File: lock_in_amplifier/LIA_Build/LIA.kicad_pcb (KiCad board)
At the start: 2 copper layers, 140 parts, among them J1 vref-in, J10 A IN COAX, J11 B IN, J13 A IN, J14 I IN COAX, J15 I IN, J16 TEST SIGNAL OUT, J17 RF_Shield_One_Piece, J18 TEST HIGH SIDE VALUE, J19 +3V3 OUT, J2 vref, J20 AMP OUT, J21 AMP OUT COAX, J22 CLK IN, J23 CLK IN COAX, J26 CLK OUT, J27 CLK OUT COAX, J3 V-IN, J30 DEMOD OUT - I, J31 DEMOD OUT I COAX, J32 DEMOD OUT Q COAX, J33 DEMOD OUT - Q, J34 DEMOD PROG, J38 RF_Shield_One_Piece, J39 BOOT, J4 GND, J42 VOCM, J46 -5V OUT, J47 +5V OUT, J48 XOUT, J5 V+IN, J6 +5V, J7 +3V3, J8 -5V, J9 B IN COAX, Q1 DMN640L, Q2 DMN640L, U1 LM358, U11 ADA2200, U6 lmp7721, U7 OP1177, U8 AD8429, U9 OP1177

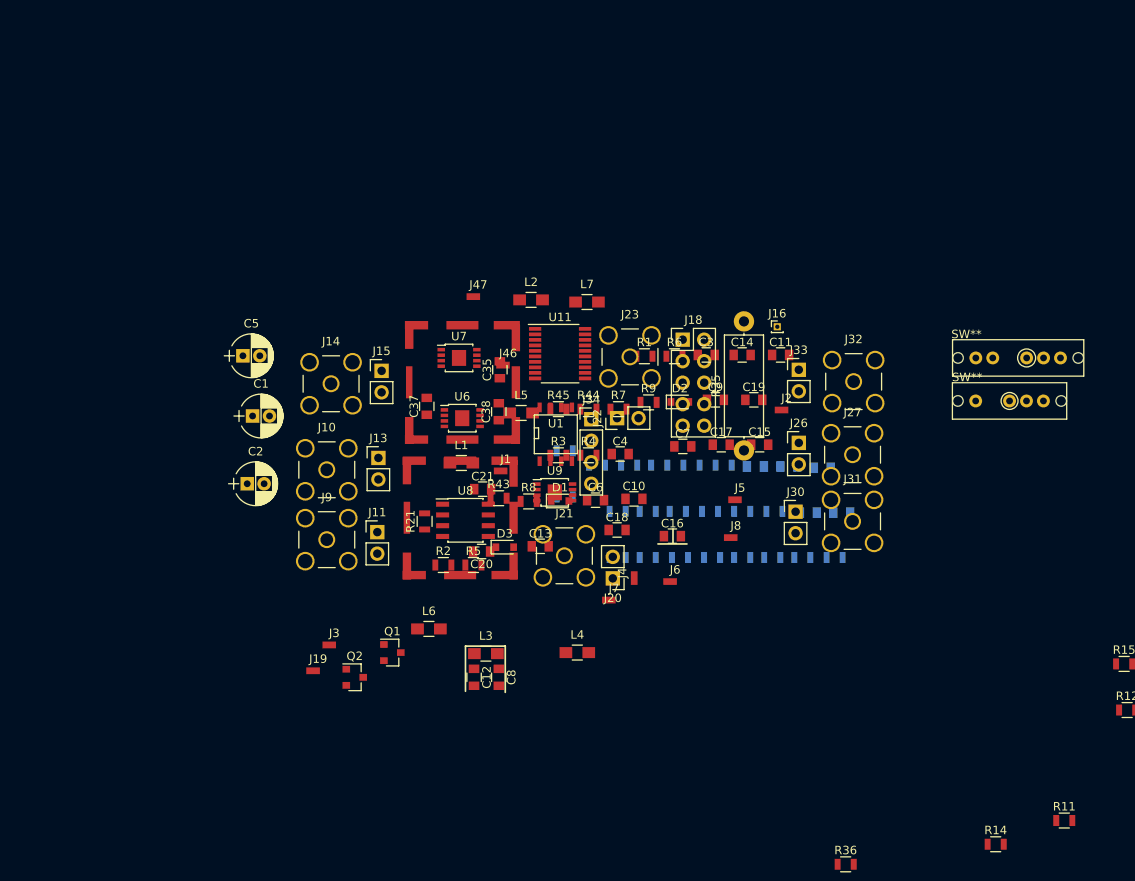
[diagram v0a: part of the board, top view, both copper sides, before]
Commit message: PLL initial implementation
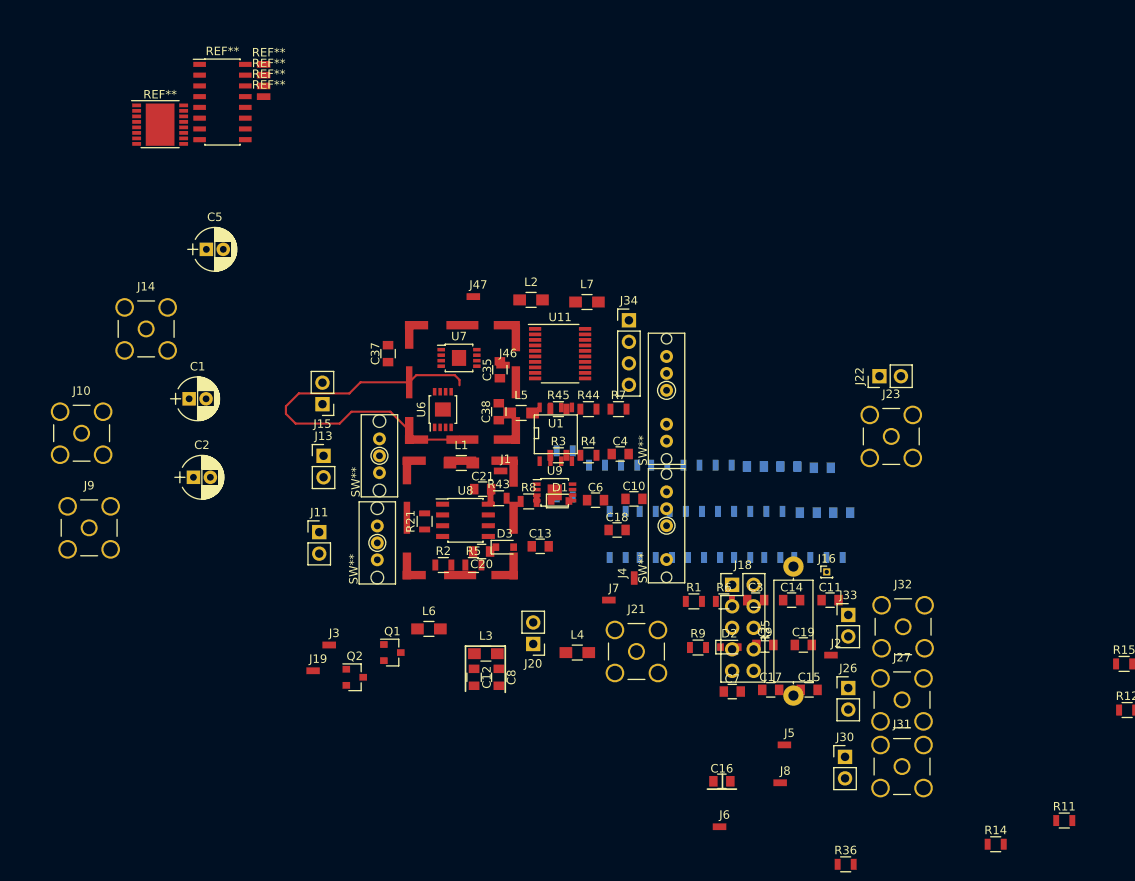
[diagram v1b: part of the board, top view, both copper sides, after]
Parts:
- added REF**: tyco_RC_0603_Probe_Pad, footprints:tyco_RCU_0603_Probe_Pad, F.Cu at (146.4, -4.06)
- added REF**: tyco_RC_0603_Probe_Pad, footprints:tyco_RCU_0603_Probe_Pad, F.Cu at (146.4, -2.79)
- added REF**: HTSSOP-16-1EP_4.4x5mm_Pitch0.65mm, Housings_SSOP:HTSSOP-16-1EP_4.4x5mm_Pitch0.65mm, F.Cu at (133.6, 2.41)
- added REF**: SOIC-16_3.9x9.9mm_Pitch1.27mm, Housings_SOIC:SOIC-16_3.9x9.9mm_Pitch1.27mm, F.Cu at (141.0, -0.25)
- added REF**: tyco_RC_0603_Probe_Pad, footprints:tyco_RCU_0603_Probe_Pad, F.Cu at (146.4, -6.60)
- added REF**: tyco_RC_0603_Probe_Pad, footprints:tyco_RCU_0603_Probe_Pad, F.Cu at (146.4, -5.33)
- added SW**: SPDT, footprints:SPDT_OS102011MS2QN1, F.Cu at (159.5, 41.5)
- added SW**: SPDT, footprints:SPDT_OS102011MS2QN1, F.Cu at (159.3, 51.8)
- moved SW** 43.1 mm to (193.4, 49.8), turned to 90 degrees
- moved SW** 41.8 mm to (193.4, 34.8), turned to 90 degrees
- moved J23 32.3 mm to (220.0, 39.2)
- moved J22 31.4 mm to (218.6, 32.1)
- moved C15 29.5 mm to (210.3, 69.2)
- moved J2 29.5 mm to (213.4, 63.2)
- moved J27 29.5 mm to (221.2, 70.4)
- moved R9 29.5 mm to (197.1, 64.2)
- moved C11 29.5 mm to (212.7, 58.6)
- moved C3 29.5 mm to (203.9, 58.6)
- moved J18 29.5 mm to (201.2, 56.8)
- moved R6 29.5 mm to (200.2, 58.7)
- moved C16 29.5 mm to (200.0, 80.0)
- moved C17 29.5 mm to (205.7, 69.2)
- moved C19 29.5 mm to (209.6, 63.9)
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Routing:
- net Net-(J17-Pad1): track 0.00 -> 46.2 mm

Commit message: started LNA test board.
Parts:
- removed REF** (x3): C_0603, Capacitors_SMD:C_0603
- removed REF** (x4): tyco_RC_0603_Probe_Pad, footprints:tyco_RCU_0603_Probe_Pad
- removed REF**: HTSSOP-16-1EP_4.4x5mm_Pitch0.65mm, Housings_SSOP:HTSSOP-16-1EP_4.4x5mm_Pitch0.65mm
- removed REF** (x2): C_0805, Capacitors_SMD:C_0805
- removed REF**: C_0402, Capacitors_SMD:C_0402
- removed REF**: SOIC-16_3.9x9.9mm_Pitch1.27mm, Housings_SOIC:SOIC-16_3.9x9.9mm_Pitch1.27mm
- removed SW** (x2): SPDT, footprints:SPDT_OS102011MS2QN1
- removed SW**: SP4T, footprints:SP4T_C&K_SS-14D0839-VG
- removed SW**: SP3T, footprints:SP3T_CK_SS-14D0839-VG
- added C25: 10pF, Capacitors_SMD:C_0805, F.Cu at (188.5, 69.4)
- added C27: 10pF, Capacitors_SMD:C_0805, F.Cu at (180.4, 74.9)
- added C31: 0.1uF, Capacitors_SMD:C_0805, F.Cu at (243.3, 87.8)
- added C32: 0.1uF, Capacitors_SMD:C_0805, F.Cu at (235.1, 98.1)
- added C33: 0.1uF, Capacitors_SMD:C_0805, F.Cu at (225.0, 108.9)
- added C34: 200pF, Capacitors_SMD:C_0805, F.Cu at (175.9, 76.6)
- added C36: 10pF, Capacitors_SMD:C_0805, F.Cu at (184.4, 69.6)
- added C39: C, Capacitors_SMD:C_0805, F.Cu at (185.6, 64.1)
- added C40: 10pF, Capacitors_SMD:C_0805, F.Cu at (176.4, 71.3)
- added C41: 270P, Capacitors_SMD:C_0805, F.Cu at (158.6, 124.8)
- added C42: 270P, Capacitors_SMD:C_0805, F.Cu at (174.4, 108.2)
- added C43: 270P, Capacitors_SMD:C_0805, F.Cu at (162.7, 119.4)
- added C44: 270P, Capacitors_SMD:C_0805, F.Cu at (182.6, 102.6)
- added C45: C, Capacitors_SMD:C_0805, F.Cu at (116.5, 49.0)
- added C46: C, Capacitors_SMD:C_0805, F.Cu at (105.5, 59.9)
- added C47: 100PF, Capacitors_SMD:C_0805, F.Cu at (101.8, 65.3)
- added C48: 0.1uF, Capacitors_SMD:C_0805, F.Cu at (98.0, 70.8)
- added C49: 0.1u, Capacitors_SMD:C_0805, F.Cu at (91.0, 76.2)
- added C50: 0.1u, Capacitors_SMD:C_0805, F.Cu at (109.4, 59.7)
- added C51: 0.1U, Capacitors_SMD:C_0805, F.Cu at (87.0, 74.5)
- added C52: 0.1U, Capacitors_SMD:C_0805, F.Cu at (112.5, 49.0)
- added C53: 0.1u, Capacitors_SMD:C_0805, F.Cu at (81.0, 87.3)
- added C54: 0.1u, Capacitors_SMD:C_0805, F.Cu at (239.5, 93.3)
- added C55: 0.1u, Capacitors_SMD:C_0805, F.Cu at (230.8, 98.1)
- added C56: 0.1u, Capacitors_SMD:C_0805, F.Cu at (120.4, 49.0)
- added C57: 0.1u, Capacitors_SMD:C_0805, F.Cu at (112.9, 54.3)
- added C58: 0.1u, Capacitors_SMD:C_0805, F.Cu at (86.0, 82.0)
- added C59: 0.1u, Capacitors_SMD:C_0805, F.Cu at (82.0, 82.0)
- added C60: C, Capacitors_SMD:C_0805, F.Cu at (109.0, 54.4)
- added D10: BAT54S, TO_SOT_Packages_SMD:SOT-23, F.Cu at (103.2, 129.5)
- added D11: BAT54S, TO_SOT_Packages_SMD:SOT-23, F.Cu at (109.1, 122.4)
- added D12: BAT54S, TO_SOT_Packages_SMD:SOT-23, F.Cu at (115.8, 110.1)
- added D13: BAT54S, TO_SOT_Packages_SMD:SOT-23, F.Cu at (103.2, 122.4)
- added D5: D, Diodes_SMD:D_0805, F.Cu at (226.7, 103.7)
- added D6: D, Diodes_SMD:D_0805, F.Cu at (207.7, 114.2)
- added D7: LED, LEDs:LED_0805, F.Cu at (231.0, 103.4)
- added D8: LED, LEDs:LED_0805, F.Cu at (85.2, 87.2)
- added D9: BAT54S, TO_SOT_Packages_SMD:SOT-23, F.Cu at (96.8, 131.7)
- added J12: POWER_IN, Pin_Headers:Pin_Header_Straight_1x03_Pitch2.54mm, F.Cu at (116.7, 98.1)
- added J24: BOOT, footprints:tyco_RCU_0603_Probe_Pad, F.Cu at (229.1, 108.2)
- added J25: VOCM, footprints:tyco_RCU_0603_Probe_Pad, F.Cu at (243.4, 92.4)
- added J28: DEMOD PROG, Pin_Headers:Pin_Header_Straight_1x04_Pitch2.54mm, F.Cu at (196.6, 103.0)
- added J29: XOUT, footprints:tyco_RCU_0603_Probe_Pad, F.Cu at (225.1, 113.5)
- added J35: rst, Pin_Headers:Pin_Header_Straight_1x02_Pitch2.54mm, F.Cu at (203.7, 107.8)
- added J36: DELAY SEL FINE, Pin_Headers:Pin_Header_Straight_1x10_Pitch2.54mm, F.Cu at (50.9, 49.8)
- added J37: DELAY SEL COARSE, Pin_Headers:Pin_Header_Straight_1x05_Pitch2.54mm, F.Cu at (64.4, 49.8)
- added J45: rst, Pin_Headers:Pin_Header_Straight_1x02_Pitch2.54mm, F.Cu at (223.3, 92.9)
- added R100: 0, Resistors_SMD:R_0805, F.Cu at (93.6, 70.9)
- added R101: 0, Resistors_SMD:R_0805, F.Cu at (101.4, 60.0)
- added R102: 0, Resistors_SMD:R_0805, F.Cu at (93.6, 65.5)
- added R103: 0, Resistors_SMD:R_0805, F.Cu at (97.1, 60.0)
- added R104: 0, Resistors_SMD:R_0805, F.Cu at (108.4, 49.1)
- added R105: R, Resistors_SMD:R_0805, F.Cu at (82.9, 76.7)
- added R106: R, Resistors_SMD:R_0805, F.Cu at (104.9, 54.6)
- added R46: 10k, Resistors_SMD:R_0805, F.Cu at (186.6, 58.8)
- added R47: 100, Resistors_SMD:R_0805, F.Cu at (176.1, 66.0)
- added R48: 1M, Resistors_SMD:R_0805, F.Cu at (172.6, 70.2)
- added R49: 10M, Resistors_SMD:R_0805, F.Cu at (190.2, 53.4)
- added R50: 10M, Resistors_SMD:R_0805, F.Cu at (163.9, 77.9)
- added R51: 100, Resistors_SMD:R_0805, F.Cu at (239.3, 88.0)
- added R52: 100, Resistors_SMD:R_0805, F.Cu at (223.0, 101.5)
- added R53: 100k, Resistors_SMD:R_0805, F.Cu at (159.3, 114.1)
- added R54: 100, Resistors_SMD:R_0805, F.Cu at (170.6, 102.9)
- added R55: 1M, Resistors_SMD:R_0805, F.Cu at (172.6, 64.8)
- added R56: 0, Resistors_SMD:R_0805, F.Cu at (178.3, 60.5)
- added R57: 0, Resistors_SMD:R_0805, F.Cu at (160.3, 76.8)
- added R58: 100, Resistors_SMD:R_0805, F.Cu at (165.9, 72.5)
- added R59: R, Resistors_SMD:R_0805, F.Cu at (183.1, 53.4)
- added R60: 10K, Resistors_SMD:R_0805, F.Cu at (156.8, 76.8)
- added R61: 0, Resistors_SMD:R_0805, F.Cu at (236.6, 49.1)
- added R62: 0, Resistors_SMD:R_0805, F.Cu at (212.9, 73.8)
- added R63: 0, Resistors_SMD:R_0805, F.Cu at (186.6, 53.4)
- added R64: 0, Resistors_SMD:R_0805, F.Cu at (183.1, 58.8)
- added R65: 0, Resistors_SMD:R_0805, F.Cu at (181.8, 64.3)
- added R66: R, Resistors_SMD:R_0805, F.Cu at (190.2, 58.8)
- added R67: 10M, Resistors_SMD:R_0805, F.Cu at (166.9, 103.8)
- added R68: 10M, Resistors_SMD:R_0805, F.Cu at (151.2, 118.9)
- added R69: 10M, Resistors_SMD:R_0805, F.Cu at (144.1, 124.0)
- added R70: 10M, Resistors_SMD:R_0805, F.Cu at (147.6, 118.6)
- added R71: 0, Resistors_SMD:R_0805, F.Cu at (97.4, 54.6)
- added R72: 0, Resistors_SMD:R_0805, F.Cu at (93.2, 60.0)
- added R73: 1M, Resistors_SMD:R_0805, F.Cu at (104.5, 49.1)
- added R74: 10K, Resistors_SMD:R_0805, F.Cu at (70.2, 84.1)
- added R75: 10K, Resistors_SMD:R_0805, F.Cu at (82.6, 71.2)
- added R76: 0, Resistors_SMD:R_0805, F.Cu at (101.0, 54.6)
- added R77: 0, Resistors_SMD:R_0805, F.Cu at (86.1, 69.2)
- added R78: 200, Resistors_SMD:R_0805, F.Cu at (73.7, 85.3)
- added R79: 10K, Resistors_SMD:R_0805, F.Cu at (89.7, 69.2)
- added R80: 10K, Resistors_SMD:R_0805, F.Cu at (101.0, 49.1)
- added R81: 10K, Resistors_SMD:R_0805, F.Cu at (66.6, 84.1)
- added R82: 10K, Resistors_SMD:R_0805, F.Cu at (97.4, 49.1)
- added R83: R, Resistors_SMD:R_0805, F.Cu at (89.7, 63.7)
- added R84: 0, Resistors_SMD:R_0805, F.Cu at (74.7, 79.8)
- added R85: 0, Resistors_SMD:R_0805, F.Cu at (85.5, 58.3)
- added R86: 0, Resistors_SMD:R_0805, F.Cu at (93.9, 49.1)
- added R87: 10K, Resistors_SMD:R_0805, F.Cu at (63.1, 82.4)
- added R88: 100K, Resistors_SMD:R_0805, F.Cu at (68.7, 70.2)
- added R89: 10K, Resistors_SMD:R_0805, F.Cu at (82.6, 65.8)
- added R90: 1M, Resistors_SMD:R_0805, F.Cu at (89.1, 58.3)
- added R91: 100, Resistors_SMD:R_0805, F.Cu at (213.4, 108.3)
- added R92: 100, Resistors_SMD:R_0805, F.Cu at (217.0, 102.9)
- added R93: 100, Resistors_SMD:R_0805, F.Cu at (227.1, 98.3)
- added R94: 10K, Resistors_SMD:R_0805, F.Cu at (93.9, 54.6)
- added R95: 10K, Resistors_SMD:R_0805, F.Cu at (86.1, 63.7)
- added R96: 0, Resistors_SMD:R_0805, F.Cu at (61.5, 87.8)
- added R97: 0, Resistors_SMD:R_0805, F.Cu at (78.3, 79.8)
- added R98: 0, Resistors_SMD:R_0805, F.Cu at (77.3, 85.3)
- added R99: 0, Resistors_SMD:R_0805, F.Cu at (97.5, 65.5)
- added S1: TEST LOW VALUE SELECT, Pin_Headers:Pin_Header_Straight_1x03_Pitch2.54mm, F.Cu at (54.1, 98.1)
- added S2: MID AMP GAIN SEL, footprints:SPDT_OS102011MS2QN1, F.Cu at (146.8, 98.7)
- added S3: REF V SEL, footprints:SPDT_OS102011MS2QN1, F.Cu at (161.9, 98.7)
- added S4: A / I SEL, footprints:SPDT_OS102011MS2QN1, F.Cu at (167.7, 50.4)
- added S5: B SEL, footprints:SPDT_OS102011MS2QN1, F.Cu at (152.2, 69.5)
- added S6: LNA GAIN SEL, footprints:SPDT_OS102011MS2QN1, F.Cu at (152.2, 58.9)
- added S9: LINE FIL SEL, footprints:SPDT_OS102011MS2QN1, F.Cu at (130.8, 115.6)
- added TP1: END AMP GAIN FB, footprints:tyco_RCU_0603_Probe_Pad, F.Cu at (147.8, 102.9)
- added TP10: OVERLOAD IND, footprints:tyco_RCU_0603_Probe_Pad, F.Cu at (207.0, 91.4)
- added TP11: TIAV+, footprints:tyco_RCU_0603_Probe_Pad, F.Cu at (180.4, 79.5)
- added TP12: GBUFFOUT, footprints:tyco_RCU_0603_Probe_Pad, F.Cu at (178.1, 48.3)
- added TP13: TIA_OUT, footprints:tyco_RCU_0603_Probe_Pad, F.Cu at (167.5, 67.1)
- added TP14: GBUFV-, footprints:tyco_RCU_0603_Probe_Pad, F.Cu at (185.3, 48.3)
- added TP15: GBUFFV+, footprints:tyco_RCU_0603_Probe_Pad, F.Cu at (160.8, 67.4)
- added TP16: TIAV-, footprints:tyco_RCU_0603_Probe_Pad, F.Cu at (188.5, 79.3)
- added TP17: CLK-IN-MIDPOINT, footprints:tyco_RCU_0603_Probe_Pad, F.Cu at (51.5, 77.8)
- added TP18: PC1, footprints:tyco_RCU_0603_Probe_Pad, F.Cu at (102.3, 74.2)
- added TP19: VCO-IN, footprints:tyco_RCU_0603_Probe_Pad, F.Cu at (56.4, 86.4)
- added TP2: MID AMP OUT, footprints:tyco_RCU_0603_Probe_Pad, F.Cu at (130.6, 119.8)
- added TP20: PC2, footprints:tyco_RCU_0603_Probe_Pad, F.Cu at (106.4, 68.7)
- added TP21: PCP, footprints:tyco_RCU_0603_Probe_Pad, F.Cu at (110.4, 64.3)
- added TP22: F/64, footprints:tyco_RCU_0603_Probe_Pad, F.Cu at (95.0, 75.5)
- added TP23: DEMOD - N - I, footprints:tyco_RCU_0603_Probe_Pad, F.Cu at (220.8, 87.1)
- added TP24: INH, footprints:tyco_RCU_0603_Probe_Pad, F.Cu at (90.0, 85.1)
- added TP25: DEM_OUT, footprints:tyco_RCU_0603_Probe_Pad, F.Cu at (57.5, 82.1)
- added TP26: PC3, footprints:tyco_RCU_0603_Probe_Pad, F.Cu at (117.9, 57.8)
- added TP27: SIGCON_OUT, footprints:tyco_RCU_0603_Probe_Pad, F.Cu at (49.2, 82.1)
- added TP28: F - COUNT, footprints:tyco_RCU_0603_Probe_Pad, F.Cu at (48.9, 86.4)
- added TP29: DEMOD - N - Q, footprints:tyco_RCU_0603_Probe_Pad, F.Cu at (208.0, 87.1)
- added TP3: GAIN AMP REF, footprints:tyco_RCU_0603_Probe_Pad, F.Cu at (143.8, 113.5)
- added TP30: F/32, footprints:tyco_RCU_0603_Probe_Pad, F.Cu at (90.0, 80.8)
- added TP31: F/2, footprints:tyco_RCU_0603_Probe_Pad, F.Cu at (114.5, 63.1)
- added TP32: COARL CLK IN, footprints:tyco_RCU_0603_Probe_Pad, F.Cu at (62.2, 65.1)
- added TP33: FMOD IN, footprints:tyco_RCU_0603_Probe_Pad, F.Cu at (69.3, 79.0)
- added TP34: FINE CLK IN, footprints:tyco_RCU_0603_Probe_Pad, F.Cu at (61.5, 69.4)
- added TP35: F/4, footprints:tyco_RCU_0603_Probe_Pad, F.Cu at (94.4, 80.8)
- added TP36: F/16, footprints:tyco_RCU_0603_Probe_Pad, F.Cu at (113.4, 58.9)
- added TP37: F/128, footprints:tyco_RCU_0603_Probe_Pad, F.Cu at (65.5, 88.7)
- added TP38: C1A, footprints:tyco_RCU_0603_Probe_Pad, F.Cu at (106.4, 64.5)
- added TP39: C1B, footprints:tyco_RCU_0603_Probe_Pad, F.Cu at (102.3, 69.9)
- added TP4: HIGH GAIN AMP OUT, footprints:tyco_RCU_0603_Probe_Pad, F.Cu at (133.1, 102.9)
- added TP40: R2, footprints:tyco_RCU_0603_Probe_Pad, F.Cu at (116.9, 53.6)
- added TP41: R1, footprints:tyco_RCU_0603_Probe_Pad, F.Cu at (121.0, 53.6)
- added TP5: CURRENT GUARD, footprints:tyco_RCU_0603_Probe_Pad, F.Cu at (153.2, 63.1)
- added TP6: CURRENT GUARD FB, footprints:tyco_RCU_0603_Probe_Pad, F.Cu at (154.5, 48.3)
- added TP7: LNA OUT, footprints:tyco_RCU_0603_Probe_Pad, F.Cu at (160.5, 71.6)
- added TP8: TIA GUARD BUFF IN, footprints:tyco_RCU_0603_Probe_Pad, F.Cu at (154.3, 52.5)
- added TP9: TIA REF, footprints:tyco_RCU_0603_Probe_Pad, F.Cu at (173.2, 59.7)
- added U10: 74HC4046A, Housings_SOIC:SOIC-16_3.9x9.9mm_Pitch1.27mm, F.Cu at (76.3, 70.1)
- added U12: LM833, Housings_SOIC:SO-8_5.3x6.2mm_Pitch1.27mm, F.Cu at (160.1, 106.2)
- added U13: ADA2200, Housings_SSOP:TSSOP-20_4.4x6.5mm_Pitch0.65mm, F.Cu at (205.9, 99.2)
- added U14: MCP6566, TO_SOT_Packages_SMD:SOT-23-5, F.Cu at (62.5, 75.8)
- added U15: MC74LCX16374, Housings_SSOP:TSSOP-48_6.1x12.5mm_Pitch0.5mm, F.Cu at (77.8, 54.8)
- added U16: LM833, Housings_SOIC:SO-8_5.3x6.2mm_Pitch1.27mm, F.Cu at (232.4, 90.5)
- added U5: 74HC4040, Housings_SSOP:TSSOP-16_4.4x5mm_Pitch0.65mm, F.Cu at (87.9, 51.0)
- U1: value LM358 -> LM833
- U7: value OP1177 -> LM833; footprint Housings_SSOP:MSOP-8-1EP_3x3mm_Pitch0.65mm -> Housings_SOIC:SO-8_5.3x6.2mm_Pitch1.27mm
- moved R12 207.4 mm to (50.4, 135.1)
- moved R10 204.0 mm to (57.8, 135.1)
- moved R13 202.0 mm to (61.4, 135.6)
- moved R11 192.9 mm to (54.3, 135.1)
- moved R15 192.0 mm to (68.5, 135.6)
- moved R14 191.9 mm to (46.5, 135.1)
- moved J32 179.1 mm to (52.5, 121.3)
- moved J16 177.4 mm to (51.4, 129.9)
- moved S8 168.1 mm to (132.7, 109.3)
- moved R35 167.1 mm to (46.4, 110.9), turned to 0 degrees
- moved S7 166.2 mm to (133.7, 98.7)
- moved J22 165.6 mm to (84.1, 128.7), turned to 0 degrees
- moved R36 156.5 mm to (64.9, 135.6)
- moved J30 156.3 mm to (66.4, 127.1)
- moved J31 155.5 mm to (70.8, 117.7)
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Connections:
- U11 pad 10: /demodulator/DEMOD_OUT_Q -> Net-(TP23-Pad1)
- U7 pad 7: Net-(C38-Pad2) -> Net-(C52-Pad1)
- U7 pad 8: Net-(U7-Pad8) -> Net-(C38-Pad2)
- U9 pad 2: Net-(R22-Pad1) -> Net-(C44-Pad1)
- U9 pad 3: Net-(S9-Pad2) -> GND
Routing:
- net Net-(J17-Pad1): track 46.2 -> 0.00 mm
